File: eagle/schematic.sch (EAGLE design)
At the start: 23 parts, among them T1 2N3904, T2 2N3904

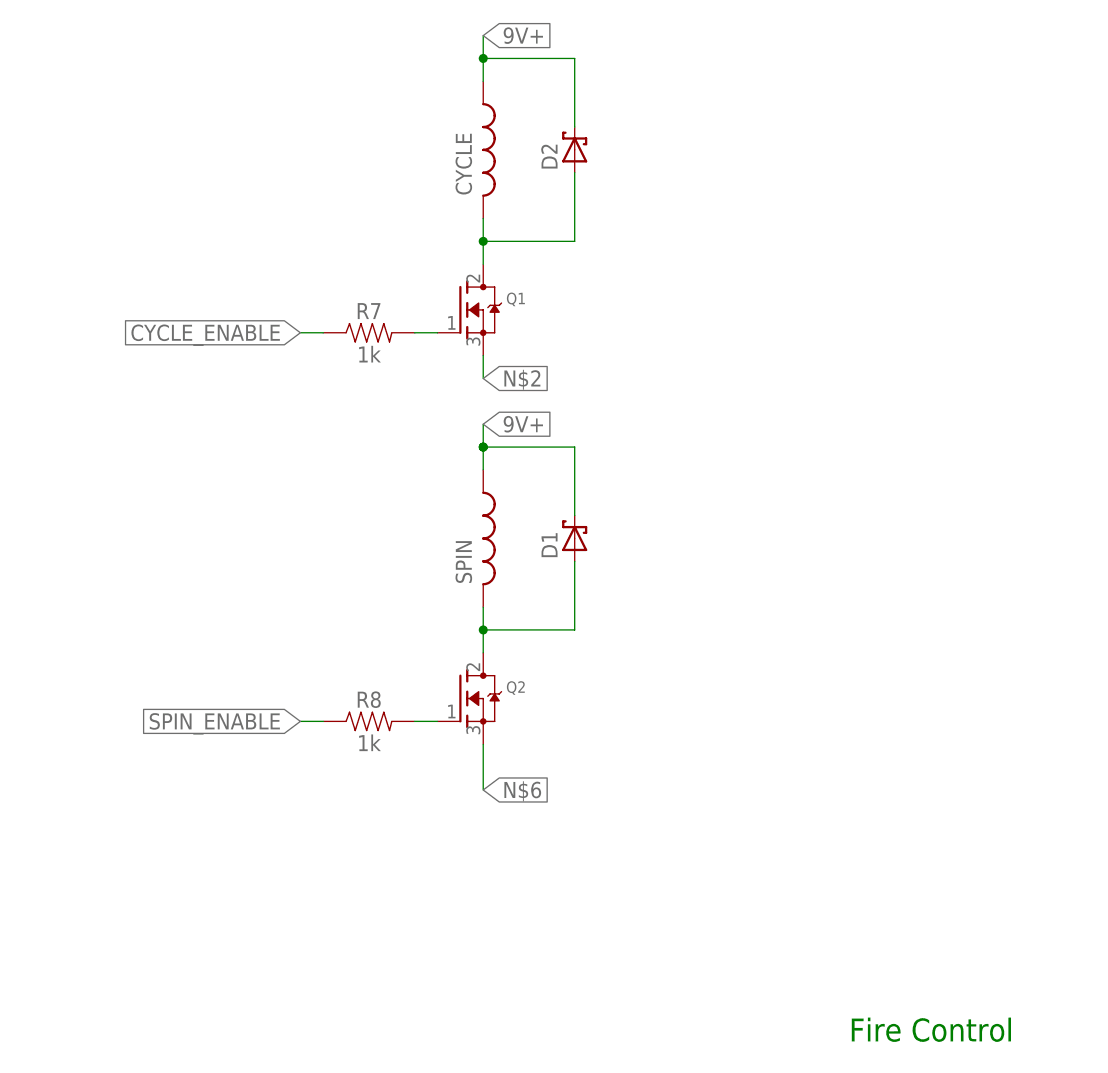
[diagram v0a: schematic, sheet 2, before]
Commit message: Add pull down to spin / cycle mosfet driver circuit
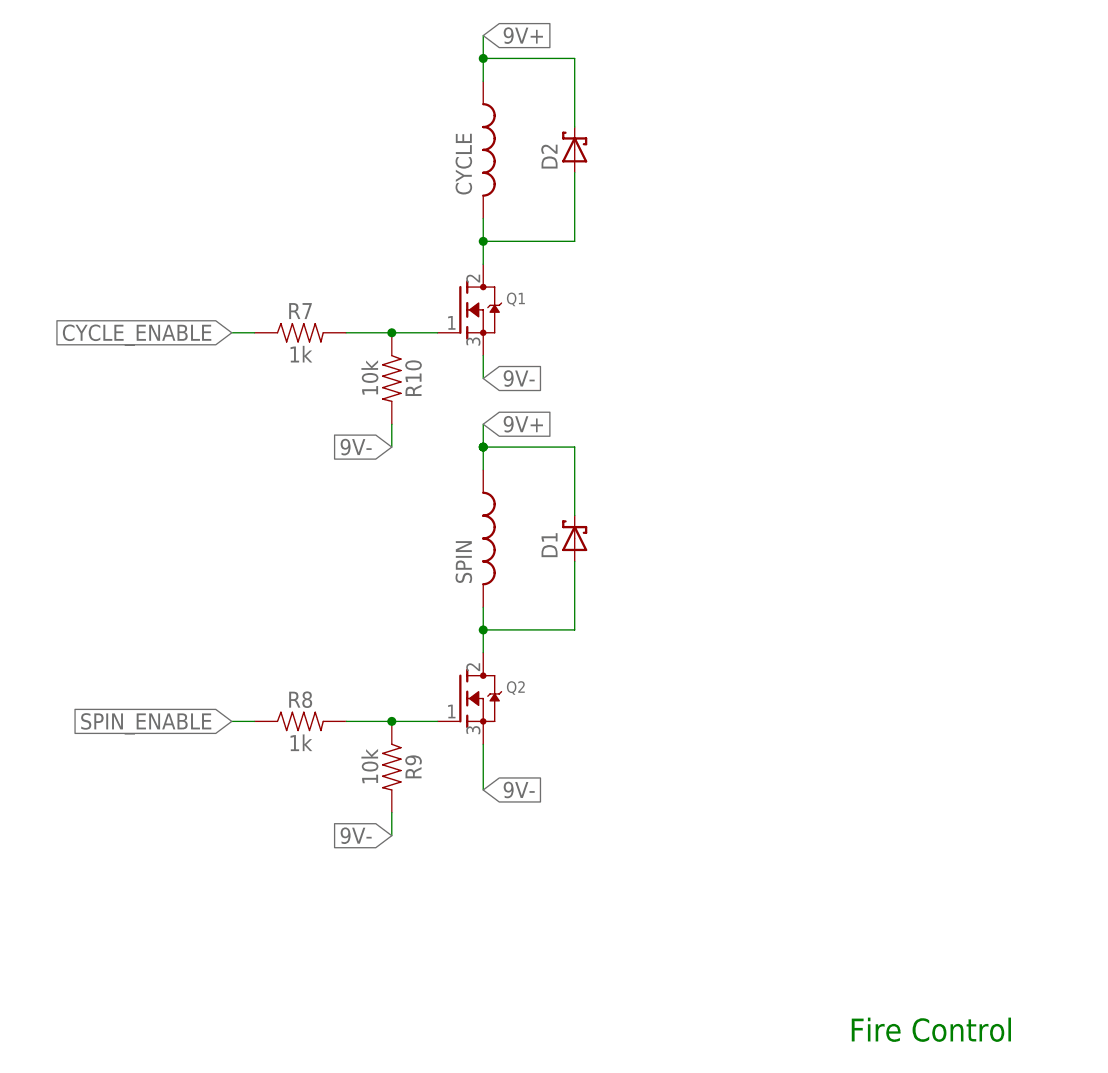
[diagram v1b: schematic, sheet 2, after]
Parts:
- added R10, R9: 10k, SparkFun-Resistors:1KOHM-HORIZ-1/4W-5%
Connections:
- removed net N$2: Q1.S
- removed net N$6: Q2.S
- net 9V-: now also Q1.S, Q2.S, R10.2, R9.2
- net N$5: now also R10.1
- net SPIN_ENABLE: now also R9.1
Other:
- moved on the sheet: R7, R8
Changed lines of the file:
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@@
 <part name="D1" library="adafruit" library_urn="urn:adsk.eagle:library:420" deviceset="SCHOTTKY-DIODE" device="CB417-15" package3d_urn="urn:adsk.eagle:package:6240685/1"/>
 <part name="D2" library="adafruit" library_urn="urn:adsk.eagle:library:420" deviceset="SCHOTTKY-DIODE" device="CB417-15" package3d_urn="urn:adsk.eagle:package:6240685/1"/>
+<part name="R9" library="SparkFun-Resistors" library_urn="urn:adsk.eagle:library:532" deviceset="1KOHM" device="-HORIZ-1/4W-5%" package3d_urn="urn:adsk.eagle:package:39658/1" value="10k"/>
+<part name="R10" library="SparkFun-Resistors" library_urn="urn:adsk.eagle:library:532" deviceset="1KOHM" device="-HORIZ-1/4W-5%" package3d_urn="urn:adsk.eagle:package:39658/1" value="10k"/>
 </parts>
 <sheets>
@@
 <attribute name="VALUE" x="0" y="31.75" size="1.27" layer="96"/>
 </instance>
-<instance part="R7" gate="G$1" x="-15.24" y="73.66">
-<attribute name="NAME" x="-15.24" y="75.184" size="1.778" layer="95" font="vector" align="bottom-center"/>
-<attribute name="VALUE" x="-15.24" y="72.136" size="1.778" layer="96" font="vector" align="top-center"/>
-</instance>
-<instance part="R8" gate="G$1" x="-15.24" y="30.48">
-<attribute name="NAME" x="-15.24" y="32.004" size="1.778" layer="95" font="vector" align="bottom-center"/>
-<attribute name="VALUE" x="-15.24" y="28.956" size="1.778" layer="96" font="vector" align="top-center"/>
+<instance part="R7" gate="G$1" x="-22.86" y="73.66">
+<attribute name="NAME" x="-22.86" y="75.184" size="1.778" layer="95" font="vector" align="bottom-center"/>
+<attribute name="VALUE" x="-22.86" y="72.136" size="1.778" layer="96" font="vector" align="top-center"/>
+</instance>
+<instance part="R8" gate="G$1" x="-22.86" y="30.48">
+<attribute name="NAME" x="-22.86" y="32.004" size="1.778" layer="95" font="vector" align="bottom-center"/>
+<attribute name="VALUE" x="-22.86" y="28.956" size="1.778" layer="96" font="vector" align="top-center"/>
 </instance>
 <instance part="D1" gate="G$1" x="7.62" y="50.8" rot="R90">
@@
 <attribute name="NAME" x="5.715" y="91.694" size="1.778" layer="95" rot="R90"/>
 <attribute name="VALUE" x="11.049" y="91.694" size="1.778" layer="96" rot="R90"/>
+</instance>
+<instance part="R9" gate="G$1" x="-12.7" y="25.4" rot="R270">
+<attribute name="NAME" x="-11.176" y="25.4" size="1.778" layer="95" font="vector" rot="R270" align="bottom-center"/>
+<attribute name="VALUE" x="-14.224" y="25.4" size="1.778" layer="96" font="vector" rot="R270" align="top-center"/>
+</instance>
+<instance part="R10" gate="G$1" x="-12.7" y="68.58" rot="R270">
+<attribute name="NAME" x="-11.176" y="68.58" size="1.778" layer="95" font="vector" rot="R270" align="bottom-center"/>
+<attribute name="VALUE" x="-14.224" y="68.58" size="1.778" layer="96" font="vector" rot="R270" align="top-center"/>
 </instance>
 </instances>
@@
 <junction x="-2.54" y="83.82"/>
 </segment>
+<segment>
+<pinref part="Q1" gate="G$1" pin="S"/>
+<wire x1="-2.54" y1="68.58" x2="-2.54" y2="71.12" width="0.1524" layer="91"/>
+<label x="-2.54" y="68.58" size="1.778" layer="95" xref="yes"/>
+</segment>
+<segment>
+<pinref part="Q2" gate="G$1" pin="S"/>
+<wire x1="-2.54" y1="22.86" x2="-2.54" y2="27.94" width="0.1524" layer="91"/>
+<label x="-2.54" y="22.86" size="1.778" layer="95" xref="yes"/>
+</segment>
+<segment>
+<pinref part="R10" gate="G$1" pin="2"/>
+<wire x1="-12.7" y1="63.5" x2="-12.7" y2="60.96" width="0.1524" layer="91"/>
+<label x="-12.7" y="60.96" size="1.778" layer="95" rot="R180" xref="yes"/>
+</segment>
+<segment>
+<pinref part="R9" gate="G$1" pin="2"/>
+<wire x1="-12.7" y1="20.32" x2="-12.7" y2="17.78" width="0.1524" layer="91"/>
+<label x="-12.7" y="17.78" size="1.778" layer="95" rot="R180" xref="yes"/>
+</segment>
 </net>
 <net name="SPIN_ENABLE" class="0">
 <segment>
-<wire x1="-7.62" y1="30.48" x2="-10.16" y2="30.48" width="0.1524" layer="91"/>
+<wire x1="-7.62" y1="30.48" x2="-12.7" y2="30.48" width="0.1524" layer="91"/>
 <pinref part="Q2" gate="G$1" pin="G"/>
 <pinref part="R8" gate="G$1" pin="2"/>
+<pinref part="R9" gate="G$1" pin="1"/>
+<wire x1="-12.7" y1="30.48" x2="-17.78" y2="30.48" width="0.1524" layer="91"/>
+<junction x="-12.7" y="30.48"/>
 </segment>
 <segment>
 <pinref part="R8" gate="G$1" pin="1"/>
-<wire x1="-20.32" y1="30.48" x2="-22.86" y2="30.48" width="0.1524" layer="91"/>
-<label x="-22.86" y="30.48" size="1.778" layer="95" rot="R180" xref="yes"/>
+<wire x1="-27.94" y1="30.48" x2="-30.48" y2="30.48" width="0.1524" layer="91"/>
+<label x="-30.48" y="30.48" size="1.778" layer="95" rot="R180" xref="yes"/>
 </segment>
 </net>
@@
 <pinref part="Q1" gate="G$1" pin="G"/>
 <pinref part="R7" gate="G$1" pin="2"/>
-<wire x1="-7.62" y1="73.66" x2="-10.16" y2="73.66" width="0.1524" layer="91"/>
-</segment>
-</net>
-<net name="CYCLE_ENABLE" class="0">
-<segment>
-<pinref part="R7" gate="G$1" pin="1"/>
-<wire x1="-22.86" y1="73.66" x2="-20.32" y2="73.66" width="0.1524" layer="91"/>
-<label x="-22.86" y="73.66" size="1.778" layer="95" rot="R180" xref="yes"/>
+<wire x1="-7.62" y1="73.66" x2="-12.7" y2="73.66" width="0.1524" layer="91"/>
+<pinref part="R10" gate="G$1" pin="1"/>
+<wire x1="-12.7" y1="73.66" x2="-17.78" y2="73.66" width="0.1524" layer="91"/>
+<junction x="-12.7" y="73.66"/>
 </segment>
 </net>
@@
 </segment>
 </net>
-<net name="N$6" class="0">
-<segment>
-<pinref part="Q2" gate="G$1" pin="S"/>
-<wire x1="-2.54" y1="22.86" x2="-2.54" y2="27.94" width="0.1524" layer="91"/>
-<label x="-2.54" y="22.86" size="1.778" layer="95" xref="yes"/>
-</segment>
-</net>
-<net name="N$2" class="0">
-<segment>
-<pinref part="Q1" gate="G$1" pin="S"/>
-<wire x1="-2.54" y1="68.58" x2="-2.54" y2="71.12" width="0.1524" layer="91"/>
-<label x="-2.54" y="68.58" size="1.778" layer="95" xref="yes"/>
-</segment>
-</net>
 <net name="N$1" class="0">
 <segment>
@@
 </segment>
 </net>
+<net name="CYCLE_ENABLE" class="0">
+<segment>
+<pinref part="R7" gate="G$1" pin="1"/>
+<wire x1="-27.94" y1="73.66" x2="-30.48" y2="73.66" width="0.1524" layer="91"/>
+<label x="-30.48" y="73.66" size="1.778" layer="95" rot="R180" xref="yes"/>
+</segment>
+</net>
